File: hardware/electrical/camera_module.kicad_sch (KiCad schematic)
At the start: 19 parts, among them J5 FFC, Q7 AO3401A, U3 TLV70028DCKR, U9 TLV70012DCKR, X2 SG-8018CA 24.0000M-TJHPA3r

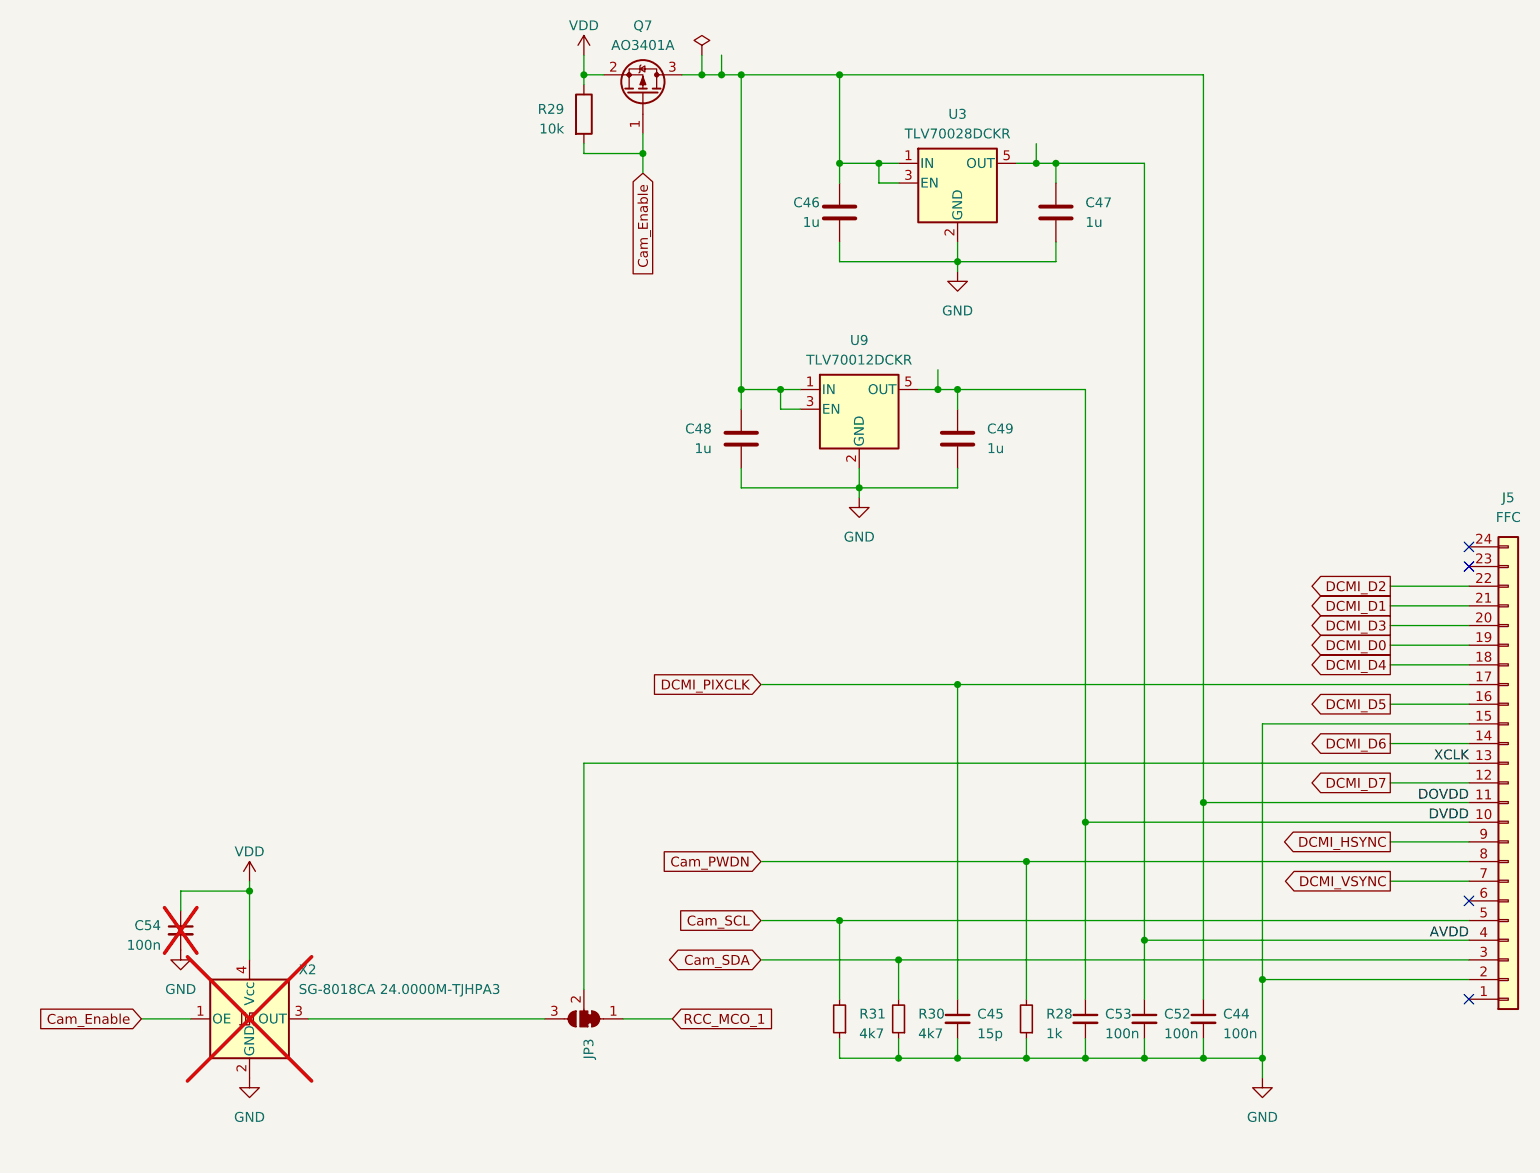
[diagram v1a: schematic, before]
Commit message: SCL and SDA pulled-up not pulled-down
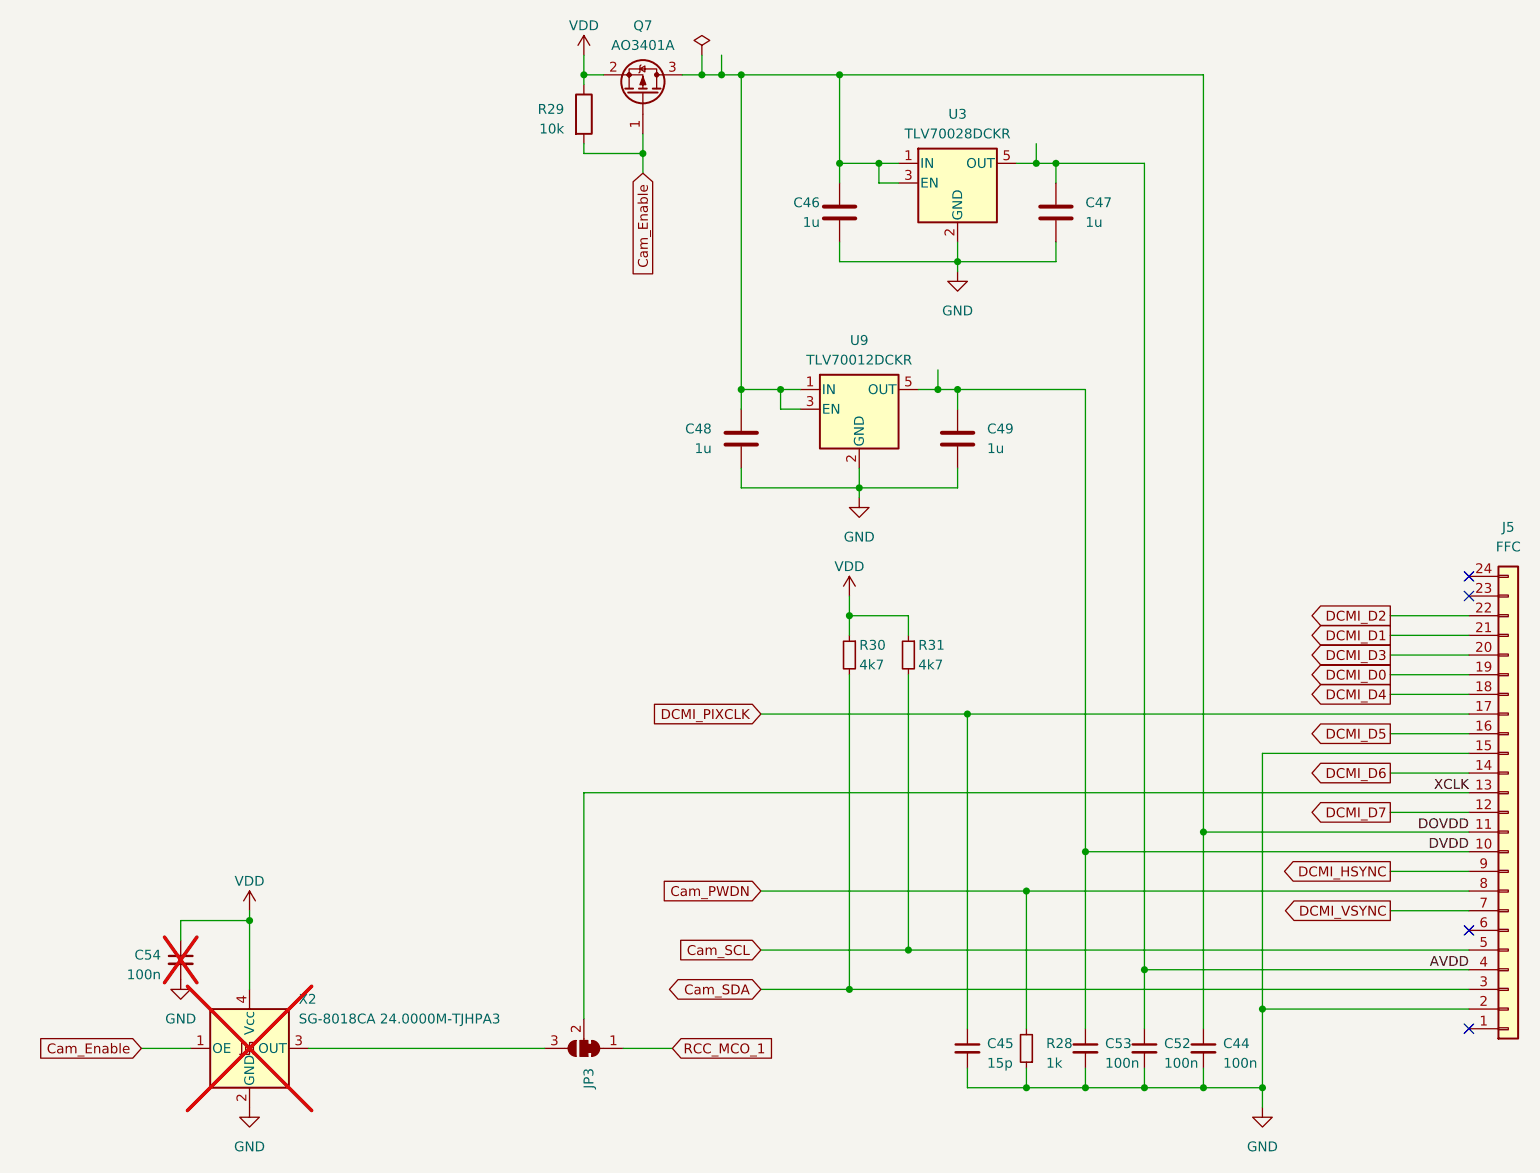
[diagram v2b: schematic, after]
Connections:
- net GND: no longer R30.1, R31.1
- net VDD: now also R30.1, R31.1
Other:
- moved on the sheet: C44, C45, C52, C53, C54, J5, JP3, R28, R30, R31, X2

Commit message: JLCPCB position and rotation adjustments
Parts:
- Q7: footprint Package_TO_SOT_SMD:SOT-23 -> 3885:JLC_SOT-23
- U3, U9: footprint Package_TO_SOT_SMD:SOT-353_SC-70-5 -> 3885:JLC_SOT-353_SC-70-5
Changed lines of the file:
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@@
       (effects (font (size 1.27 1.27)))
     )
-    (property "Footprint" "Package_TO_SOT_SMD:SOT-353_SC-70-5" (at 184.15 30.48 0)
+    (property "Footprint" "3885:JLC_SOT-353_SC-70-5" (at 184.15 30.48 0)
       (effects (font (size 1.27 1.27) italic) hide)
     )
@@
       (effects (font (size 1.27 1.27)))
     )
-    (property "Footprint" "Package_TO_SOT_SMD:SOT-23" (at 141.605 21.59 0)
+    (property "Footprint" "3885:JLC_SOT-23" (at 141.605 21.59 0)
       (effects (font (size 1.27 1.27) italic) (justify left) hide)
     )
@@
       (effects (font (size 1.27 1.27)))
     )
-    (property "Footprint" "Package_TO_SOT_SMD:SOT-353_SC-70-5" (at 171.45 59.69 0)
+    (property "Footprint" "3885:JLC_SOT-353_SC-70-5" (at 171.45 59.69 0)
       (effects (font (size 1.27 1.27) italic) hide)
     )
